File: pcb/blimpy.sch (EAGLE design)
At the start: 72 parts, among them J1 MICRO-USB, J4 3-PIN SMD, J5 3-PIN SMD, J6 3-PIN SMD, J7 3-PIN SMD, Q1 mmbt2222, Q2 mmbt2222, Q3 DMG3415U, U1 RGB, U10 MAX17048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

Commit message: updated
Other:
- note added: "TODO - Connect IMU to MC - Connect Servos to MC - Connect IOs to MC - Expose unused GPIOs - Check all components - Replace Switch with something Standard - Replace USB with USB-C"
- note removed: "TODO - Connect IMU to MC - Connect Servos to MC - Connect H-Bridges to IOs - Connect IOs to MC - Expose unused GPIOs - Check all components"
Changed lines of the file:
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@@
 - Connect IMU to MC
 - Connect Servos to MC
-- Connect H-Bridges to IOs
 - Connect IOs to MC
 - Expose unused GPIOs
-- Check all components</text>
+- Check all components
+- Replace Switch with something Standard
+- Replace USB with USB-C</text>
 <text x="342.9" y="106.68" size="1.778" layer="94">GPIO Expander 1
 I2C Address: 0x3E</text>
@@
 </sheet>
 </sheets>
+<errors>
+</errors>
 </schematic>
 </drawing>

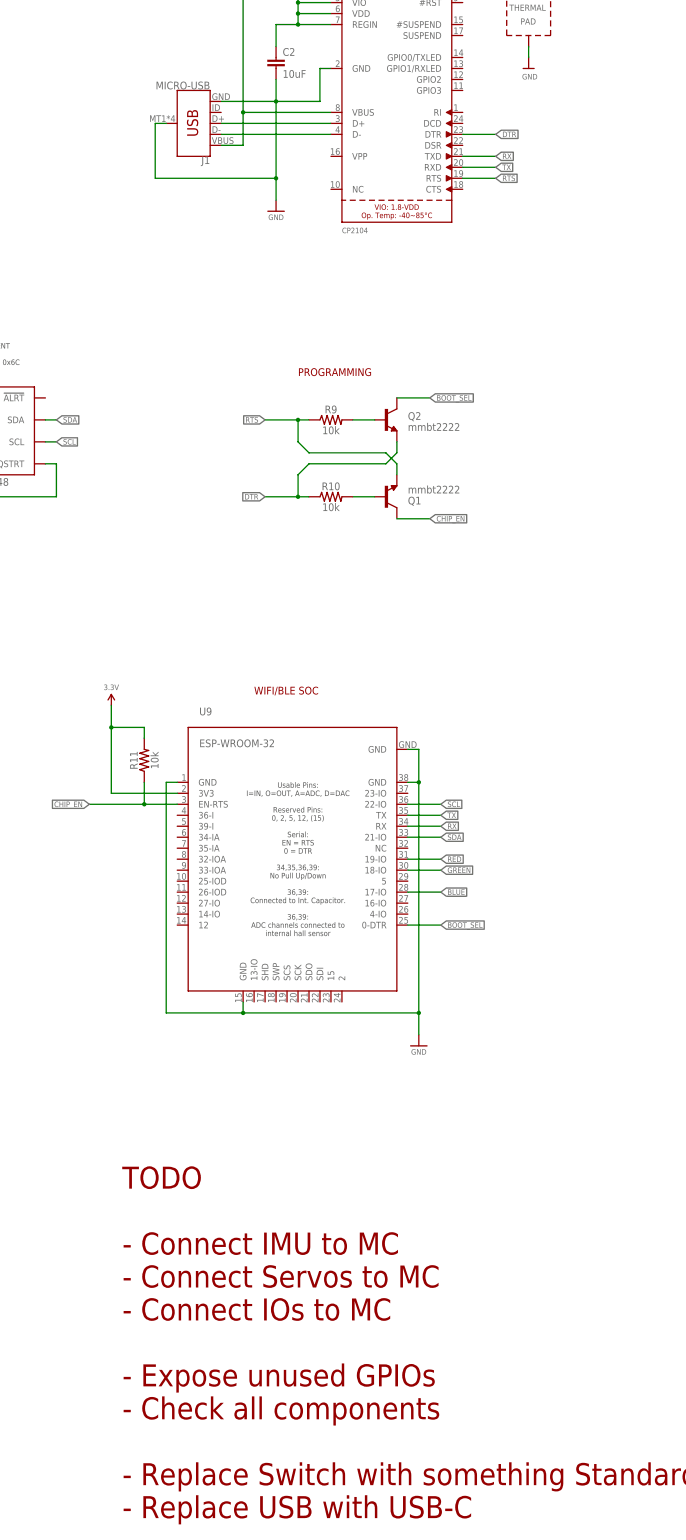
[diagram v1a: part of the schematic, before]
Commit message: replaced usb micro with usb c connector
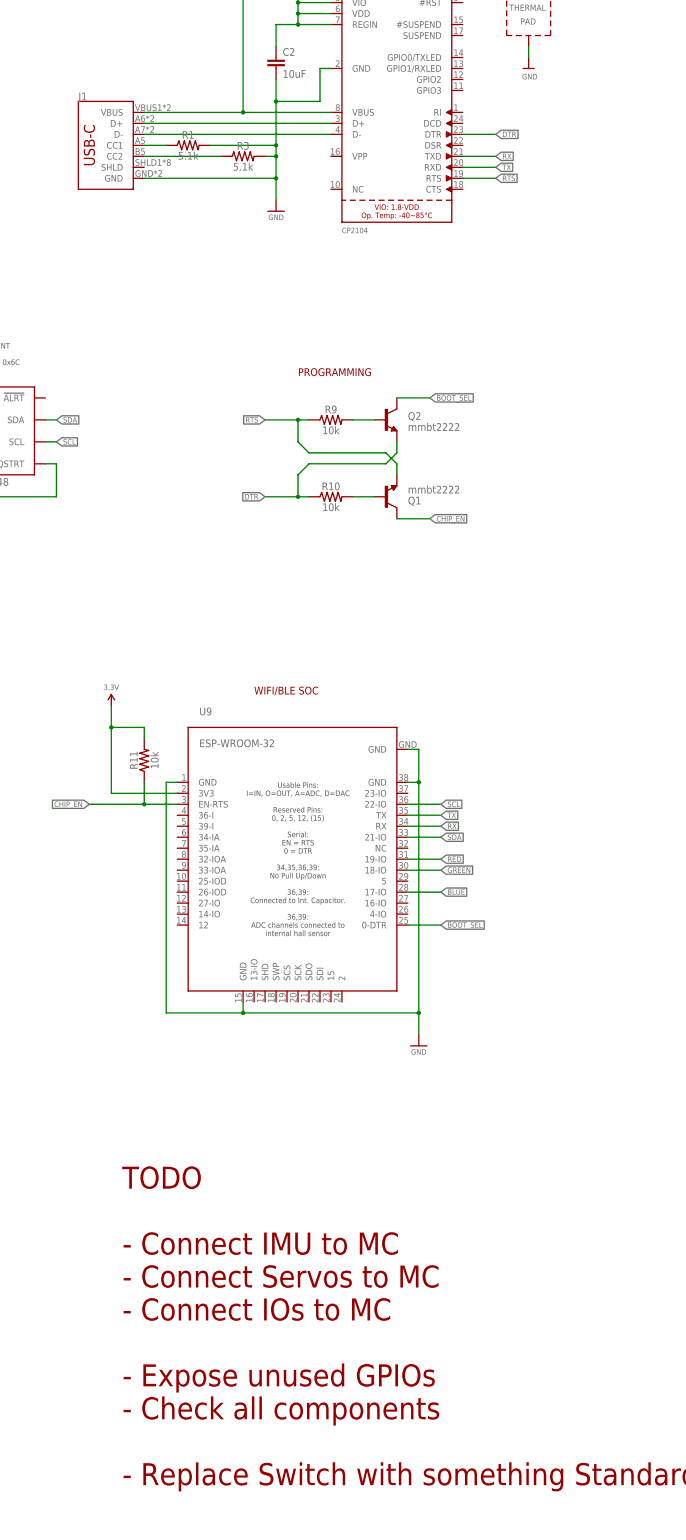
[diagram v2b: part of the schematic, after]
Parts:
- added R1, R3: 5.1k, SparkFun-Resistors:1KOHM-0603-1/10W-1%
- J1: value MICRO-USB -> (none); device SparkFun-Connectors:USB_MICRO-B_SMT -> SparkFun-Connectors:USB_C16PIN
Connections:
- new net N$17: J1.CC2, R3.1
- new net N$5: J1.CC1, R1.1
- net GND: now also R1.2, R3.2; no longer J1.SHIELD
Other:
- note added: "TODO - Connect IMU to MC - Connect Servos to MC - Connect IOs to MC - Expose unused GPIOs - Check all components - Replace Switch with something Standard"
- note removed: "TODO - Connect IMU to MC - Connect Servos to MC - Connect IOs to MC - Expose unused GPIOs - Check all components - Replace Switch with something Standard - Replace USB with USB-C"
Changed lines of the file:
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@@
 <part name="R10" library="SparkFun-Resistors" deviceset="10KOHM" device="-0603-1/10W-1%" value="10k"/>
 <part name="R11" library="SparkFun-Resistors" deviceset="10KOHM" device="-0603-1/10W-1%" value="10k"/>
-<part name="J1" library="SparkFun-Connectors" deviceset="USB_MICRO-B" device="_SMT" value="MICRO-USB"/>
 <part name="HB1" library="adafruit" library_urn="urn:adsk.eagle:library:420" deviceset="TB6612FNG" device="" package3d_urn="urn:adsk.eagle:package:6240758/1"/>
 <part name="C5" library="SparkFun-Capacitors" deviceset="0.1UF" device="-0603-25V-5%" value="0.1uF"/>
@@
 <part name="U10" library="SparkFun-IC-Power" library_urn="urn:adsk.eagle:library:526" deviceset="MAX17048" device="DFN8" package3d_urn="urn:adsk.eagle:package:39085/1" value="MAX17048"/>
 <part name="C11" library="SparkFun-Capacitors" library_urn="urn:adsk.eagle:library:510" deviceset="0.1UF" device="-0603-25V-5%" package3d_urn="urn:adsk.eagle:package:37414/1" value="0.1uF"/>
+<part name="J1" library="SparkFun-Connectors" deviceset="USB_C" device="16PIN"/>
+<part name="R1" library="SparkFun-Resistors" library_urn="urn:adsk.eagle:library:532" deviceset="1KOHM" device="-0603-1/10W-1%" package3d_urn="urn:adsk.eagle:package:39650/1" value="5.1k"/>
+<part name="R3" library="SparkFun-Resistors" library_urn="urn:adsk.eagle:library:532" deviceset="1KOHM" device="-0603-1/10W-1%" package3d_urn="urn:adsk.eagle:package:39650/1" value="5.1k"/>
 </parts>
 <sheets>
@@
 - Expose unused GPIOs
 - Check all components
-- Replace Switch with something Standard
-- Replace USB with USB-C</text>
+- Replace Switch with something Standard</text>
 <text x="342.9" y="106.68" size="1.778" layer="94">GPIO Expander 1
 I2C Address: 0x3E</text>
@@
 <attribute name="VALUE" x="166.624" y="35.56" size="1.778" layer="96" font="vector" rot="R90" align="top-center"/>
 </instance>
-<instance part="J1" gate="G$1" x="177.8" y="182.88" smashed="yes" rot="R180">
-<attribute name="VALUE" x="180.34" y="190.754" size="1.778" layer="96" font="vector" rot="R180" align="top-left"/>
-<attribute name="NAME" x="180.34" y="175.26" size="1.778" layer="95" font="vector" rot="R180"/>
-</instance>
 <instance part="HB1" gate="G$1" x="485.14" y="198.12" smashed="yes">
 <attribute name="NAME" x="472.44" y="221.488" size="1.778" layer="95"/>
@@
 <attribute name="NAME" x="108.204" y="109.601" size="1.778" layer="95" font="vector"/>
 <attribute name="VALUE" x="108.204" y="104.521" size="1.778" layer="96" font="vector"/>
+</instance>
+<instance part="J1" gate="J1" x="152.4" y="177.8" smashed="yes">
+<attribute name="VALUE" x="149.86" y="165.354" size="1.778" layer="96" font="vector" rot="MR180" align="top-left"/>
+<attribute name="NAME" x="149.86" y="188.214" size="1.778" layer="95" font="vector"/>
+</instance>
+<instance part="R1" gate="G$1" x="175.26" y="177.8" smashed="yes">
+<attribute name="NAME" x="175.26" y="179.324" size="1.778" layer="95" font="vector" align="bottom-center"/>
+<attribute name="VALUE" x="175.26" y="176.276" size="1.778" layer="96" font="vector" align="top-center"/>
+</instance>
+<instance part="R3" gate="G$1" x="187.96" y="175.26" smashed="yes">
+<attribute name="NAME" x="187.96" y="176.784" size="1.778" layer="95" font="vector" align="bottom-center"/>
+<attribute name="VALUE" x="187.96" y="173.736" size="1.778" layer="96" font="vector" align="top-center"/>
 </instance>
 </instances>
@@
 </segment>
 <segment>
-<pinref part="J1" gate="G$1" pin="SHIELD"/>
-<wire x1="167.64" y1="170.18" x2="167.64" y2="182.88" width="0.1524" layer="91"/>
-<wire x1="167.64" y1="182.88" x2="170.18" y2="182.88" width="0.1524" layer="91"/>
-<pinref part="J1" gate="G$1" pin="GND"/>
-<wire x1="167.64" y1="170.18" x2="195.58" y2="170.18" width="0.1524" layer="91"/>
 <pinref part="U7" gate="G$1" pin="GND"/>
 <wire x1="208.28" y1="195.58" x2="205.74" y2="195.58" width="0.1524" layer="91"/>
@@
 <pinref part="C2" gate="G$1" pin="2"/>
 <wire x1="195.58" y1="193.04" x2="195.58" y2="187.96" width="0.1524" layer="91"/>
-<wire x1="195.58" y1="187.96" x2="195.58" y2="170.18" width="0.1524" layer="91"/>
+<wire x1="195.58" y1="187.96" x2="195.58" y2="177.8" width="0.1524" layer="91"/>
+<wire x1="195.58" y1="177.8" x2="195.58" y2="175.26" width="0.1524" layer="91"/>
+<wire x1="195.58" y1="175.26" x2="195.58" y2="170.18" width="0.1524" layer="91"/>
+<wire x1="195.58" y1="170.18" x2="195.58" y2="165.1" width="0.1524" layer="91"/>
 <wire x1="205.74" y1="187.96" x2="195.58" y2="187.96" width="0.1524" layer="91"/>
 <junction x="195.58" y="187.96"/>
+<pinref part="GND9" gate="1" pin="GND"/>
+<pinref part="J1" gate="J1" pin="GND"/>
+<wire x1="165.1" y1="170.18" x2="195.58" y2="170.18" width="0.1524" layer="91"/>
 <junction x="195.58" y="170.18"/>
-<wire x1="182.88" y1="187.96" x2="195.58" y2="187.96" width="0.1524" layer="91"/>
-<pinref part="GND9" gate="1" pin="GND"/>
-<wire x1="195.58" y1="170.18" x2="195.58" y2="165.1" width="0.1524" layer="91"/>
+<pinref part="R3" gate="G$1" pin="2"/>
+<wire x1="193.04" y1="175.26" x2="195.58" y2="175.26" width="0.1524" layer="91"/>
+<junction x="195.58" y="175.26"/>
+<pinref part="R1" gate="G$1" pin="2"/>
+<wire x1="180.34" y1="177.8" x2="195.58" y2="177.8" width="0.1524" layer="91"/>
+<junction x="195.58" y="177.8"/>
 </segment>
 <segment>
@@
 <segment>
 <pinref part="U7" gate="G$1" pin="D+"/>
-<wire x1="182.88" y1="182.88" x2="208.28" y2="182.88" width="0.1524" layer="91"/>
-<pinref part="J1" gate="G$1" pin="D+"/>
+<pinref part="J1" gate="J1" pin="D+"/>
+<wire x1="208.28" y1="182.88" x2="165.1" y2="182.88" width="0.1524" layer="91"/>
 </segment>
 </net>
@@
 <segment>
 <pinref part="U7" gate="G$1" pin="D-"/>
-<wire x1="182.88" y1="180.34" x2="208.28" y2="180.34" width="0.1524" layer="91"/>
-<pinref part="J1" gate="G$1" pin="D-"/>
+<pinref part="J1" gate="J1" pin="D-"/>
+<wire x1="165.1" y1="180.34" x2="208.28" y2="180.34" width="0.1524" layer="91"/>
 </segment>
 </net>
@@
 <pinref part="U7" gate="G$1" pin="VBUS"/>
 <wire x1="187.96" y1="185.42" x2="208.28" y2="185.42" width="0.1524" layer="91"/>
-<wire x1="182.88" y1="177.8" x2="187.96" y2="177.8" width="0.1524" layer="91"/>
-<wire x1="187.96" y1="177.8" x2="187.96" y2="185.42" width="0.1524" layer="91"/>
+<pinref part="SUPPLY1" gate="G$1" pin="V_USB"/>
+<pinref part="J1" gate="J1" pin="VBUS"/>
 <wire x1="187.96" y1="185.42" x2="187.96" y2="215.9" width="0.1524" layer="91"/>
+<wire x1="165.1" y1="185.42" x2="187.96" y2="185.42" width="0.1524" layer="91"/>
 <junction x="187.96" y="185.42"/>
-<pinref part="J1" gate="G$1" pin="VBUS"/>
-<pinref part="SUPPLY1" gate="G$1" pin="V_USB"/>
 </segment>
 <segment>
@@
 </segment>
 </net>
+<net name="N$5" class="0">
+<segment>
+<pinref part="J1" gate="J1" pin="CC1"/>
+<pinref part="R1" gate="G$1" pin="1"/>
+<wire x1="165.1" y1="177.8" x2="170.18" y2="177.8" width="0.1524" layer="91"/>
+</segment>
+</net>
+<net name="N$17" class="0">
+<segment>
+<pinref part="J1" gate="J1" pin="CC2"/>
+<pinref part="R3" gate="G$1" pin="1"/>
+<wire x1="165.1" y1="175.26" x2="182.88" y2="175.26" width="0.1524" layer="91"/>
+</segment>
+</net>

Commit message: updated
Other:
- note added: "TODO - Connect IMU to MC - Connect Servos to MC - Connect IOs to MC - Expose unused GPIOs - Expose important GPIOs - Check all components"
- note removed: "TODO - Connect IMU to MC - Connect Servos to MC - Connect IOs to MC - Expose unused GPIOs - Check all components - Replace Switch with something Standard"
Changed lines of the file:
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@@
 - Connect IOs to MC
 - Expose unused GPIOs
-- Check all components
-- Replace Switch with something Standard</text>
+- Expose important GPIOs
+- Check all components</text>
 <text x="342.9" y="106.68" size="1.778" layer="94">GPIO Expander 1
 I2C Address: 0x3E</text>

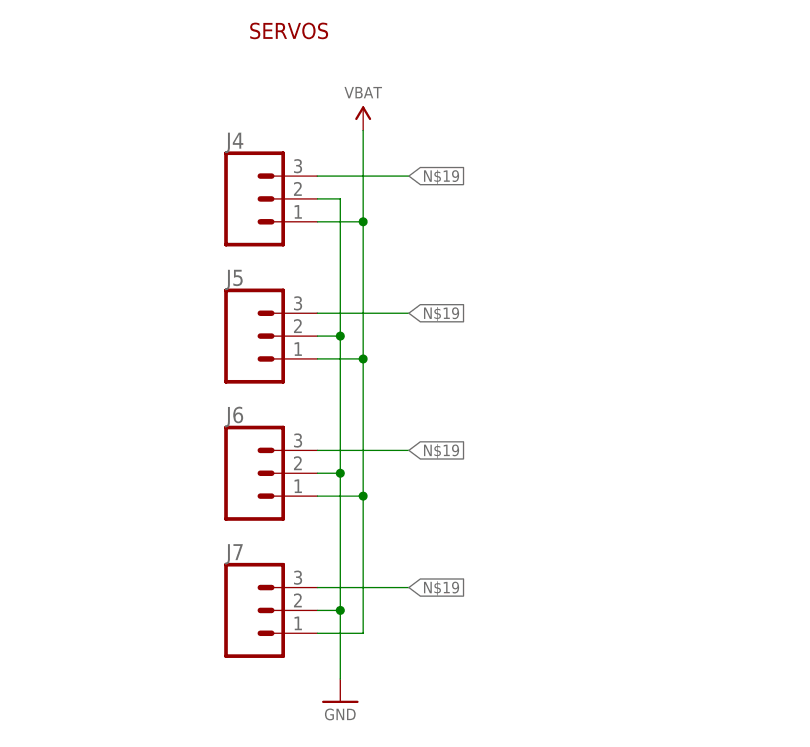
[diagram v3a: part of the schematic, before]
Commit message: fixed servo pins
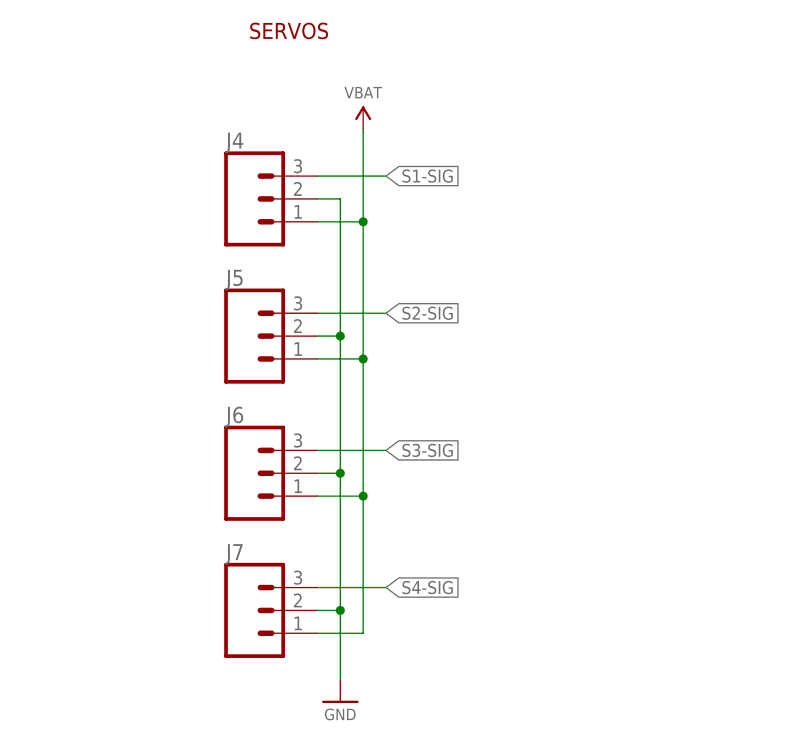
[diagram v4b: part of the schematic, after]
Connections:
- removed net N$19: J4.3, J5.3, J6.3, J7.3
- new net S1-SIG: J4.3
- new net S2-SIG: J5.3
- new net S3-SIG: J6.3
- new net S4-SIG: J7.3
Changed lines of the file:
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@@
-</segment>
-</net>
-<net name="N$19" class="0">
-<segment>
-<pinref part="J4" gate="J$1" pin="3"/>
-<wire x1="53.34" y1="-66.04" x2="63.5" y2="-66.04" width="0.1524" layer="91"/>
-<label x="63.5" y="-66.04" size="1.27" layer="95" xref="yes"/>
-</segment>
-<segment>
-<pinref part="J5" gate="J$1" pin="3"/>
-<wire x1="53.34" y1="-81.28" x2="63.5" y2="-81.28" width="0.1524" layer="91"/>
-<label x="63.5" y="-81.28" size="1.27" layer="95" xref="yes"/>
-</segment>
-<segment>
-<pinref part="J6" gate="J$1" pin="3"/>
-<wire x1="53.34" y1="-96.52" x2="63.5" y2="-96.52" width="0.1524" layer="91"/>
-<label x="63.5" y="-96.52" size="1.27" layer="95" xref="yes"/>
-</segment>
-<segment>
-<pinref part="J7" gate="J$1" pin="3"/>
-<wire x1="53.34" y1="-111.76" x2="63.5" y2="-111.76" width="0.1524" layer="91"/>
-<label x="63.5" y="-111.76" size="1.27" layer="95" xref="yes"/>
 </segment>
 </net>
@@
 </segment>
 </net>
+<net name="S1-SIG" class="0">
+<segment>
+<pinref part="J4" gate="J$1" pin="3"/>
+<wire x1="53.34" y1="-66.04" x2="60.96" y2="-66.04" width="0.1524" layer="91"/>
+<label x="60.96" y="-66.04" size="1.4224" layer="95" xref="yes"/>
+</segment>
+</net>
+<net name="S2-SIG" class="0">
+<segment>
+<pinref part="J5" gate="J$1" pin="3"/>
+<wire x1="53.34" y1="-81.28" x2="60.96" y2="-81.28" width="0.1524" layer="91"/>
+<label x="60.96" y="-81.28" size="1.4224" layer="95" xref="yes"/>
+</segment>
+</net>
+<net name="S3-SIG" class="0">
+<segment>
+<pinref part="J6" gate="J$1" pin="3"/>
+<wire x1="53.34" y1="-96.52" x2="60.96" y2="-96.52" width="0.1524" layer="91"/>
+<label x="60.96" y="-96.52" size="1.4224" layer="95" xref="yes"/>
+</segment>
+</net>
+<net name="S4-SIG" class="0">
+<segment>
+<pinref part="J7" gate="J$1" pin="3"/>
+<wire x1="53.34" y1="-111.76" x2="60.96" y2="-111.76" width="0.1524" layer="91"/>
+<label x="60.96" y="-111.76" size="1.4224" layer="95" xref="yes"/>
+</segment>
+</net>
